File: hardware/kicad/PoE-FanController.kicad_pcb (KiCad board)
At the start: 2 copper layers, 82 x 78 mm, 33 parts, among them J2 FAN1, J3 FAN2, J4 FAN3, J5 FAN4, J6 Molex_KK254_3pin, J8 Waveshare_ESP32P4POEETH, U1 LM2587-12

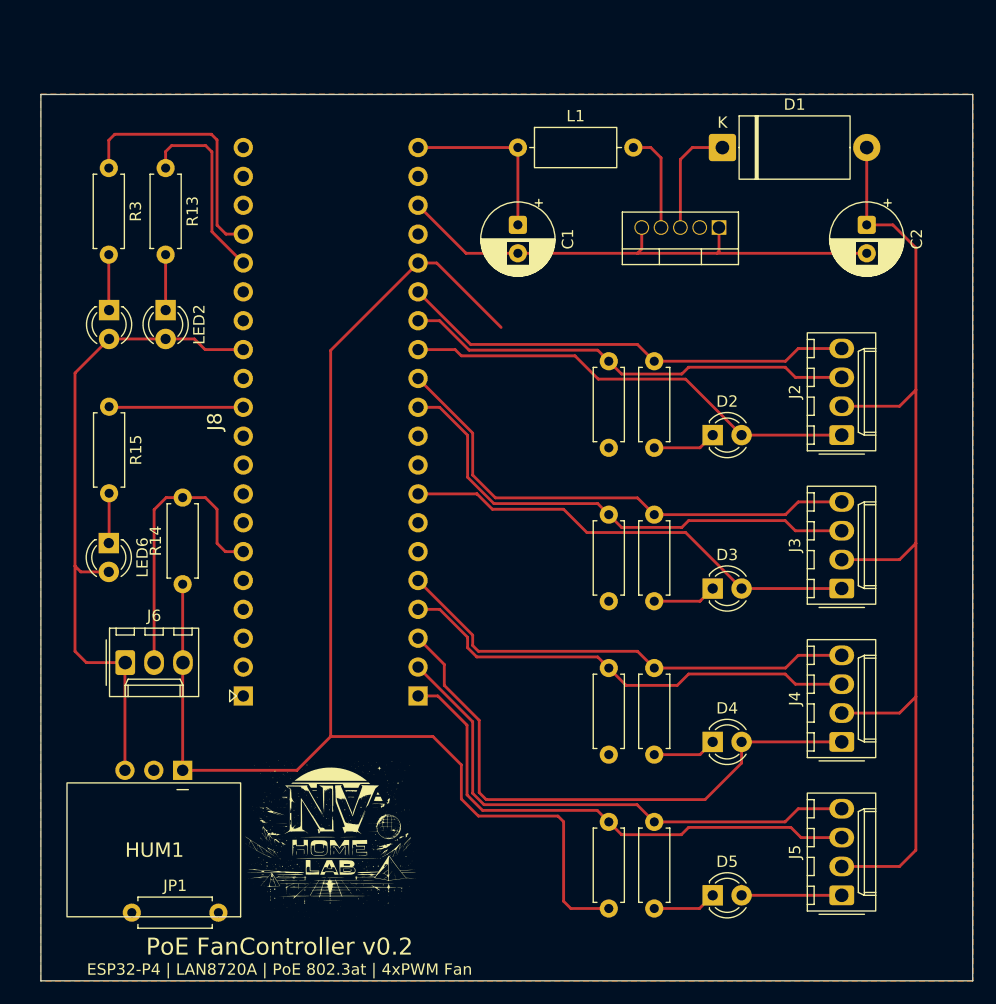
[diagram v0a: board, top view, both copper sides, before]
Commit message: pcb: add JP2/JP3/JP4 jumpers on +3V3 net
All three placed at y=84mm (bottom area), horizontal 7.62mm pitch.
User to reposition as needed during manual routing.

Co-authored-by: Copilot <223556219+Copilot@users.noreply.github.com>
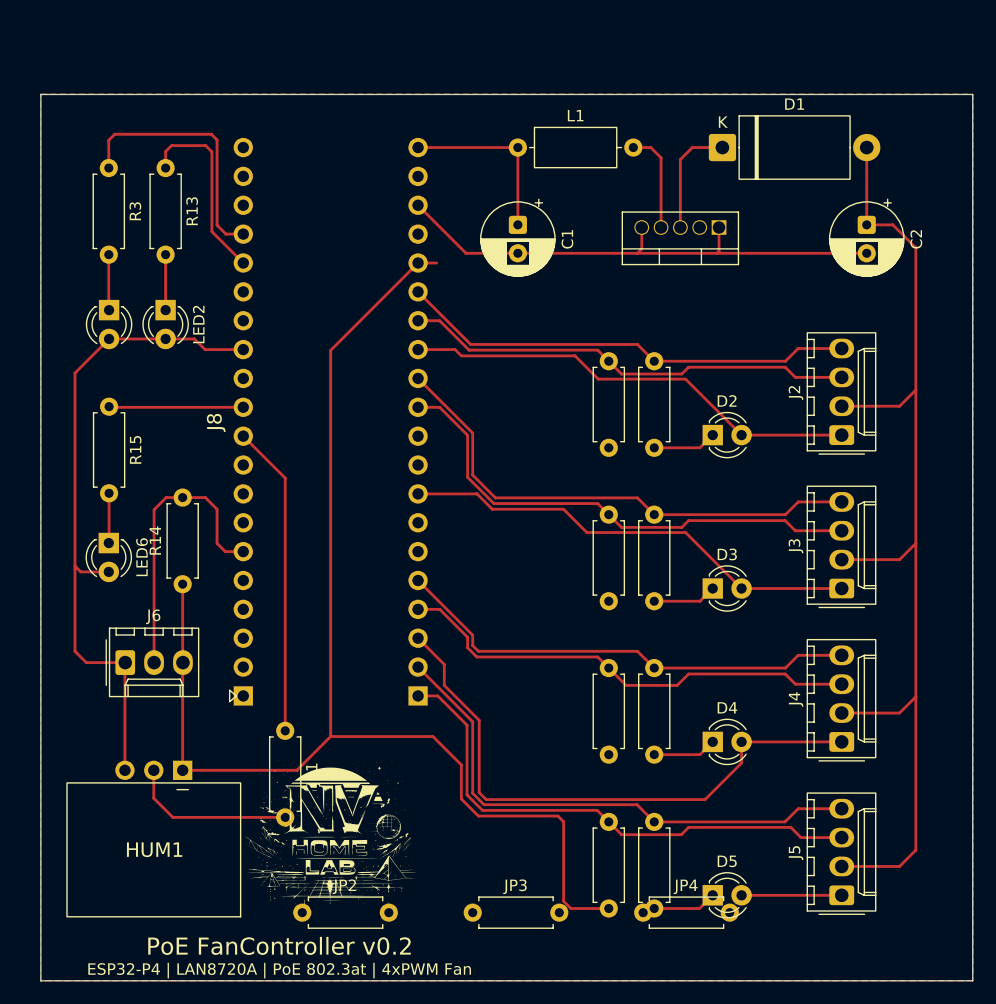
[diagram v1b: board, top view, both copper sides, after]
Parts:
- added JP2: Jumper, R_Axial_DIN0207_L6.3mm_D2.5mm_P7.62mm_Horizontal, F.Cu at (35.0, 84.0)
- added JP3: Jumper, R_Axial_DIN0207_L6.3mm_D2.5mm_P7.62mm_Horizontal, F.Cu at (50.0, 84.0)
- added JP4: Jumper, R_Axial_DIN0207_L6.3mm_D2.5mm_P7.62mm_Horizontal, F.Cu at (65.0, 84.0)
- moved JP1 20.9 mm to (33.5, 68.0), turned to -90 degrees
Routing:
- net DHT11_DATA: track 0.00 -> 42.2 mm
- net +3V3: track 121.8 -> 113.8 mm

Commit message: pcb: flip JP1-JP4 jumpers to back of board (B.Cu)
Co-authored-by: Copilot <223556219+Copilot@users.noreply.github.com>
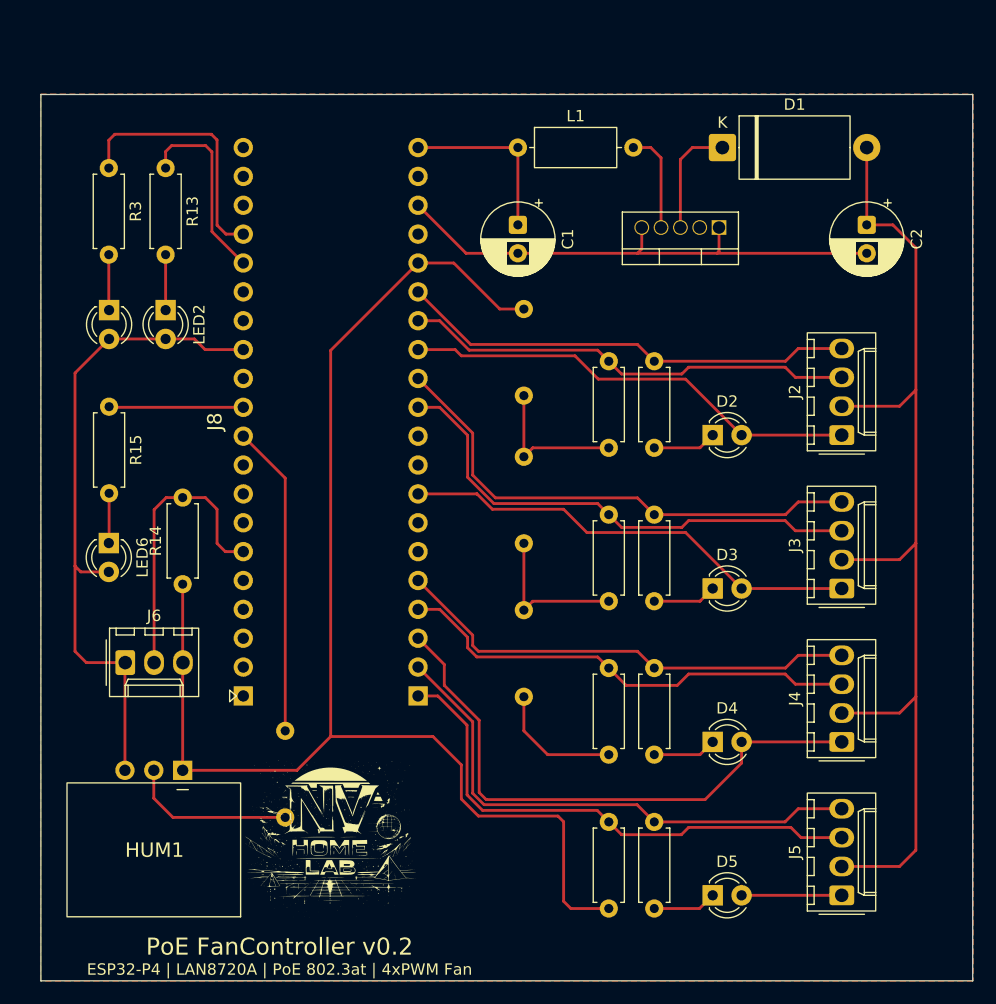
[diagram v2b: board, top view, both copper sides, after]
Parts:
- JP1, JP2, JP3, JP4: moved to B.Cu
- moved JP2 49.5 mm to (54.5, 38.5), turned to 90 degrees
- moved JP3 32.8 mm to (54.5, 51.5), turned to 90 degrees
- moved JP4 21.7 mm to (54.5, 65.0), turned to 90 degrees
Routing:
- net +3V3: track 113.8 -> 161.3 mm

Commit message: pcb: set default and minimum track width to 0.4mm
- Default netclass track width: 0.4mm
- Minimum track width: 0.4mm
- Active width index set to 0.4mm preset
- Prevents interactive router from drawing sub-0.4mm traces

Co-authored-by: Copilot <223556219+Copilot@users.noreply.github.com>
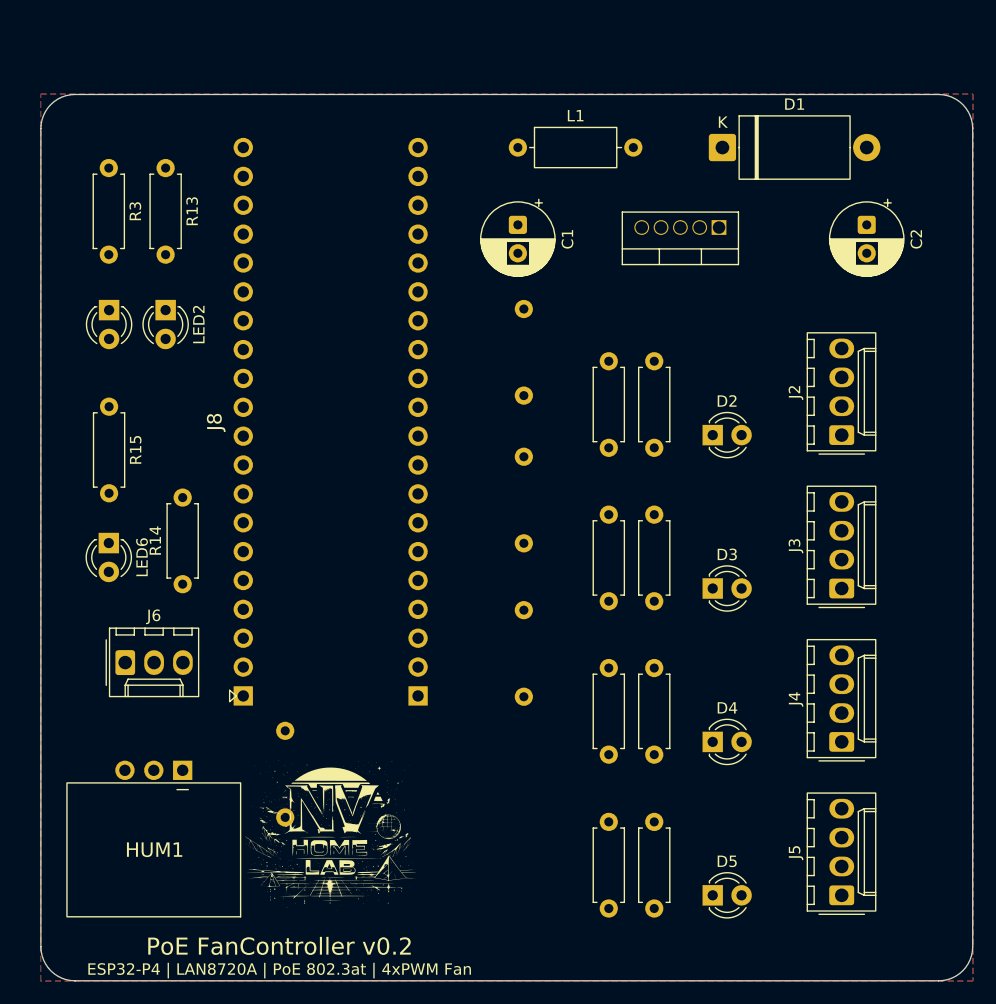
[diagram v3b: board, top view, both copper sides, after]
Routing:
- net GND: track 246.4 -> 0.00 mm
- net +3V3: track 161.3 -> 0.00 mm
- net +12V: track 93.4 -> 0.00 mm
- net FAN4_PWM: track 47.1 -> 0.00 mm
- net FAN4_TACH: track 46.6 -> 0.00 mm
- net FAN2_PWM: track 44.9 -> 0.00 mm
- net FAN2_TACH: track 44.4 -> 0.00 mm
- net DHT11_DATA: track 42.2 -> 0.00 mm
- net FAN3_PWM: track 41.5 -> 0.00 mm
- net FAN3_TACH: track 41.4 -> 0.00 mm
- net FAN1_PWM: track 40.3 -> 0.00 mm
- net FAN1_TACH: track 39.8 -> 0.00 mm
- net DS18B20_DATA: track 25.5 -> 0.00 mm
- net PWR_LED: track 22.5 -> 0.00 mm
- net BOOST_SW: track 19.1 -> 0.00 mm
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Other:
- outline, holes or cut-outs redrawn

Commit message: schematic+pcb: fix U1 FB pin (pad 4) net from BOOST_SW to +12V
For the LM2587-12, the FB/SENSE pin (pin 4) must sense the +12V output
rail, not the switching node. Tying FB to BOOST_SW was incorrect.

Co-authored-by: Copilot <223556219+Copilot@users.noreply.github.com>
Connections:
- U1 pad 4: BOOST_SW -> +12V
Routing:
- net GND: track 0.00 -> 284.0 mm
- net +3V3: track 0.00 -> 162.4 mm
- net +12V: track 0.00 -> 93.4 mm
- net +5V: track 0.00 -> 57.6 mm
- net FAN4_TACH: track 0.00 -> 47.3 mm
- net FAN4_PWM: track 0.00 -> 47.1 mm
- net FAN2_PWM: track 0.00 -> 44.9 mm
- net FAN2_TACH: track 0.00 -> 44.1 mm
- net DHT11_DATA: track 0.00 -> 42.2 mm
- net FAN3_TACH: track 0.00 -> 41.2 mm
- net FAN3_PWM: track 0.00 -> 40.9 mm
- net FAN1_TACH: track 0.00 -> 40.5 mm
- net FAN1_PWM: track 0.00 -> 40.3 mm
- net DS18B20_DATA: track 0.00 -> 25.5 mm
- net PWR_LED: track 0.00 -> 22.5 mm
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
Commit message: pcb: manual routing complete — single layer F.Cu
- All nets fully connected (0 unconnected items)
- Trace width 0.4mm (signals) enforced throughout
- F.Cu GND copper pour with 0.2mm clearance and thermal relief
- Rounded board corners (R=3mm) on Edge.Cuts
- JP1-JP4 wire jumpers placed on B.Cu for cross-pour bridges
- 0 DRC errors; 8 non-blocking warnings (silkscreen/library)

Co-authored-by: Copilot <223556219+Copilot@users.noreply.github.com>
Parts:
- moved U1 7.18 mm to (64.5, 23.5), turned to 0 degrees
- moved G*** 5.15 mm to (42.0, 80.0)
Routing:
- net +5V: track 57.6 -> 32.2 mm
- net +3V3: track 162.4 -> 185.3 mm
- net +12V: track 93.4 -> 110.4 mm
- net DHT11_DATA: track 42.2 -> 49.8 mm
- net BOOST_SW: track 19.1 -> 14.8 mm
- net GND: track 284.0 -> 284.5 mm

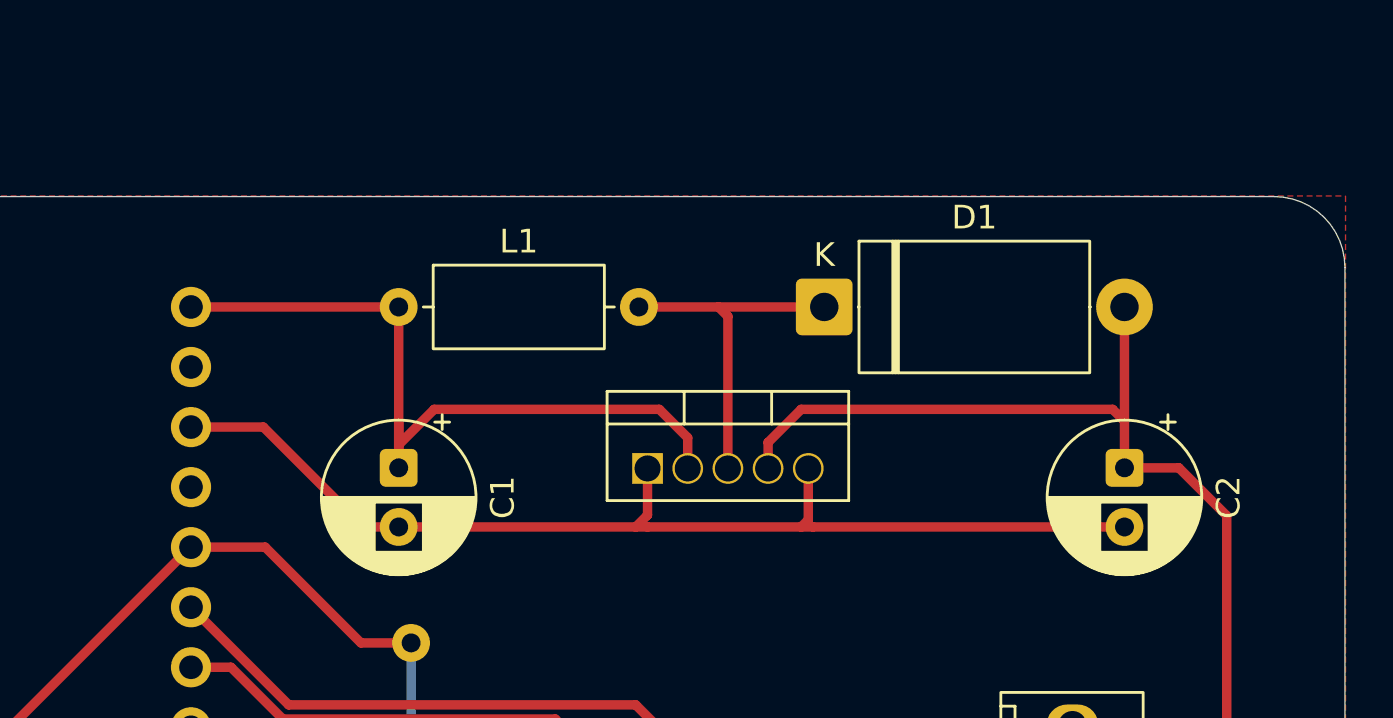
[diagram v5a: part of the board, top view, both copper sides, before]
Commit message: hw(layout): replace discrete boost stage with U_BOOST in PCB (T006)
- Delete footprints U1/L1/D1/C1/C2 and 30 associated track segments via pcbnew
- Remove BOOST_SW net tracks (net no longer exists in schematic)
- Add Custom:DC-Boost-Module as U_BOOST at (48.0, 20.0) mm F.Cu
- All 4 pads in x=33.19-56mm zone: Pad1=44.19, Pad2=46.73, Pad3=49.27, Pad4=51.81
- Net assignments: Pad1=+5V, Pad2=GND, Pad3=+12V, Pad4=GND
- Route power traces (1.0mm F.Cu):
    +5V:  Pad1 -> J8 pad 40 (45.19, 16.67)
    GND:  Pad2/Pad4 -> J8 pad 38 (45.19, 21.75)
    +12V: Pad3 -> +12V spine at (89.00, 25.50) -> fan headers J2-J5
- Update import_netlist.py: remove U1/L1/D1/C1/C2, add U_BOOST entries
- Update route_board.py: remove BOOST_SW from POWER_NETS

Closes #183
Task: T006
Issue: #183

Co-authored-by: Copilot <223556219+Copilot@users.noreply.github.com>
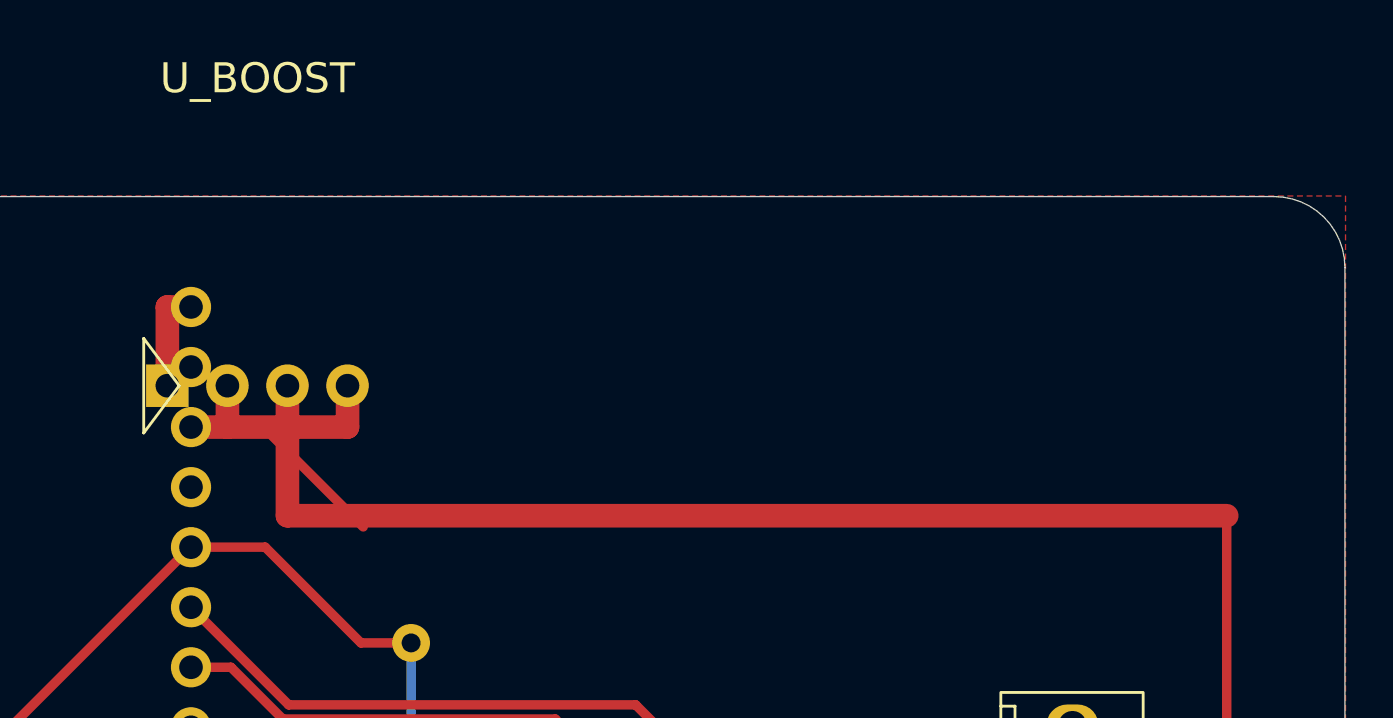
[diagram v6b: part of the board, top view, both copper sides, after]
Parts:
- removed C1, C2: 100uF_25V, Capacitor_THT:CP_Radial_D6.3mm_P2.50mm
- removed D1: 1N5822, Diode_THT:D_DO-27_P12.70mm_Horizontal
- removed L1: 100uH, Inductor_THT:L_Axial_L7.0mm_D3.3mm_P10.16mm_Horizontal_Fastron_MICC
- removed U1: LM2587-12, Package_TO_SOT_THT:TO-220-5_Vertical
- added U_BOOST: DC-Boost-Module, DC-Boost-Module, F.Cu at (48.0, 20.0)
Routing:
- net +5V: track 32.2 -> 4.33 mm
- net GND: track 284.5 -> 257.1 mm
- net +12V: track 110.4 -> 126.7 mm
- net BOOST_SW: track 14.8 -> 0.00 mm
